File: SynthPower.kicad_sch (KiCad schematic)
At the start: 22 parts, among them IC1 BUF634AIDDAR, IC2 BUF634AIDDAR, IC3 BUF634AIDDAR, J39 Jack-DC, U50 TPS560200, U51 LM1117MP-3.3

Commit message: more work...
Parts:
- C2, C3, C4, C5: footprint Capacitor_SMD:C_0805_2012Metric_Pad1.18x1.45mm_HandSolder -> Capacitor_SMD:C_0805_2012Metric
- C6, C7: footprint Capacitor_SMD:C_0805_2012Metric_Pad1.18x1.45mm_HandSolder -> Capacitor_SMD:C_0603_1608Metric
- R? (x4): footprint Resistor_SMD:R_0805_2012Metric -> Resistor_SMD:R_0603_1608Metric
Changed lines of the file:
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@@
       (effects (font (size 1.27 1.27)))
     )
-    (property "Footprint" "Capacitor_SMD:C_0805_2012Metric_Pad1.18x1.45mm_HandSolder" (at 86.6648 153.035 0)
+    (property "Footprint" "Capacitor_SMD:C_0805_2012Metric" (at 86.6648 153.035 0)
       (effects (font (size 1.27 1.27)) hide)
     )
@@
       (effects (font (size 1.27 1.27)))
     )
-    (property "Footprint" "Capacitor_SMD:C_0805_2012Metric_Pad1.18x1.45mm_HandSolder" (at 86.6648 160.655 0)
+    (property "Footprint" "Capacitor_SMD:C_0805_2012Metric" (at 86.6648 160.655 0)
       (effects (font (size 1.27 1.27)) hide)
     )
@@
       (effects (font (size 1.27 1.27)))
     )
-    (property "Footprint" "Capacitor_SMD:C_0805_2012Metric_Pad1.18x1.45mm_HandSolder" (at 99.3648 153.035 0)
+    (property "Footprint" "Capacitor_SMD:C_0603_1608Metric" (at 99.3648 153.035 0)
       (effects (font (size 1.27 1.27)) hide)
     )
@@
       (effects (font (size 1.27 1.27)))
     )
-    (property "Footprint" "Capacitor_SMD:C_0805_2012Metric_Pad1.18x1.45mm_HandSolder" (at 222.5548 114.3 0)
+    (property "Footprint" "Capacitor_SMD:C_0603_1608Metric" (at 222.5548 114.3 0)
       (effects (font (size 1.27 1.27)) hide)
     )
@@
       (effects (font (size 1.27 1.27)) (justify right))
     )
-    (property "Footprint" "Resistor_SMD:R_0805_2012Metric" (at 66.929 44.196 90)
+    (property "Footprint" "Resistor_SMD:R_0603_1608Metric" (at 66.929 44.196 90)
       (effects (font (size 1.27 1.27)) hide)
     )
@@
       (effects (font (size 1.27 1.27)))
     )
-    (property "Footprint" "Capacitor_SMD:C_0805_2012Metric_Pad1.18x1.45mm_HandSolder" (at 256.2098 114.3 0)
+    (property "Footprint" "Capacitor_SMD:C_0805_2012Metric" (at 256.2098 114.3 0)
       (effects (font (size 1.27 1.27)) hide)
     )
@@
       (effects (font (size 1.27 1.27)))
     )
-    (property "Footprint" "Capacitor_SMD:C_0805_2012Metric_Pad1.18x1.45mm_HandSolder" (at 93.0148 153.035 0)
+    (property "Footprint" "Capacitor_SMD:C_0805_2012Metric" (at 93.0148 153.035 0)
       (effects (font (size 1.27 1.27)) hide)
     )
@@
       (effects (font (size 1.27 1.27)))
     )
-    (property "Footprint" "Resistor_SMD:R_0805_2012Metric" (at 201.676 125.984 90)
+    (property "Footprint" "Resistor_SMD:R_0603_1608Metric" (at 201.676 125.984 90)
       (effects (font (size 1.27 1.27)) hide)
     )
@@
       (effects (font (size 1.27 1.27)))
     )
-    (property "Footprint" "Capacitor_SMD:C_0805_2012Metric_Pad1.18x1.45mm_HandSolder" (at 209.8548 114.3 0)
+    (property "Footprint" "Capacitor_SMD:C_0805_2012Metric" (at 209.8548 114.3 0)
       (effects (font (size 1.27 1.27)) hide)
     )
@@
       (effects (font (size 1.27 1.27)))
     )
-    (property "Footprint" "Capacitor_SMD:C_0805_2012Metric_Pad1.18x1.45mm_HandSolder" (at 99.3648 160.655 0)
+    (property "Footprint" "Capacitor_SMD:C_0603_1608Metric" (at 99.3648 160.655 0)
       (effects (font (size 1.27 1.27)) hide)
     )
@@
       (effects (font (size 1.27 1.27)))
     )
-    (property "Footprint" "Capacitor_SMD:C_0805_2012Metric_Pad1.18x1.45mm_HandSolder" (at 216.2048 114.3 0)
+    (property "Footprint" "Capacitor_SMD:C_0805_2012Metric" (at 216.2048 114.3 0)
       (effects (font (size 1.27 1.27)) hide)
     )
@@
       (effects (font (size 1.27 1.27)) (justify right))
     )
-    (property "Footprint" "Resistor_SMD:R_0805_2012Metric" (at 66.929 51.816 90)
+    (property "Footprint" "Resistor_SMD:R_0603_1608Metric" (at 66.929 51.816 90)
       (effects (font (size 1.27 1.27)) hide)
     )
@@
       (effects (font (size 1.27 1.27)))
     )
-    (property "Footprint" "Resistor_SMD:R_0805_2012Metric" (at 201.676 118.364 90)
+    (property "Footprint" "Resistor_SMD:R_0603_1608Metric" (at 201.676 118.364 90)
       (effects (font (size 1.27 1.27)) hide)
     )
@@
       (effects (font (size 1.27 1.27)))
     )
-    (property "Footprint" "Capacitor_SMD:C_0805_2012Metric_Pad1.18x1.45mm_HandSolder" (at 93.0148 160.655 0)
+    (property "Footprint" "Capacitor_SMD:C_0805_2012Metric" (at 93.0148 160.655 0)
       (effects (font (size 1.27 1.27)) hide)
     )
@@
       (effects (font (size 1.27 1.27)))
     )
-    (property "Footprint" "Capacitor_SMD:C_0805_2012Metric_Pad1.18x1.45mm_HandSolder" (at 263.1948 114.3 0)
-      (effects (font (size 1.27 1.27)) hide)
-    )
+    (property "Footprint" "Capacitor_SMD:C_0805_2012Metric" (at 263.1948 114.3 0)
+      (effects (font (size 1.27 1.27)) hide)
+    )

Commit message: finishing schematic 1.0
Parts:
- added C?: 470nF, Capacitor_SMD:C_0805_2012Metric, symbol Device:C
- added C?: 4.7uF, Capacitor_SMD:C_0805_2012Metric, symbol Device:C
- added TP10, TP11, TP12, TP13, TP7, TP8, TP9: TestPoint, TestPoint:TestPoint_Plated_Hole_D2.0mm, symbol Connector:TestPoint
- J44: renamed from J39; footprint (none) -> Connector_BarrelJack:BarrelJack_CUI_PJ-063AH_Horizontal
- U51: renamed from IC2; footprint SOIC127P600X170-9N -> Package_SO:SOIC-8_3.9x4.9mm_P1.27mm
- U52: renamed from IC3; footprint SOIC127P600X170-9N -> Package_SO:SOIC-8_3.9x4.9mm_P1.27mm
- renumbered C2 to C?, C3 to C?, C6 to C?, C4 to C?, C7 to C?, C5 to C?, IC1 to U50, U50 to U53, U51 to U54
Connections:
- net +12V: now also TP7.1
- net +3V3: now also TP13.1
- net +5V: now also C?.2, C?.2, TP12.1
- net -12V: now also TP9.1
- net GNDD: now also C?.1, C?.1, TP11.1
- net GNDREF: now also TP8.1
- net GNDS: now also TP10.1

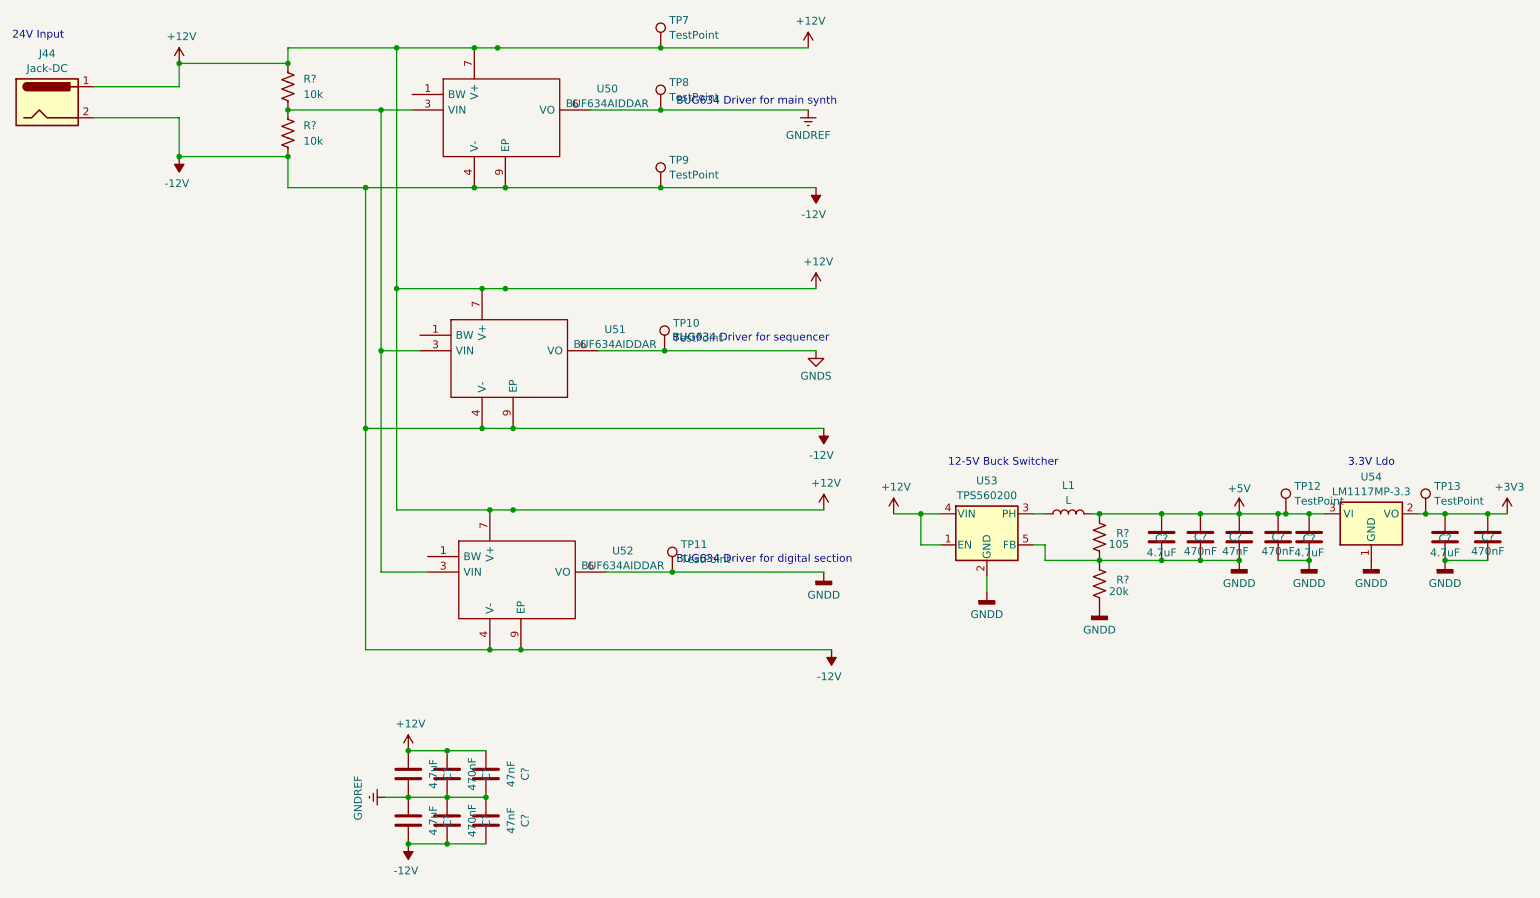
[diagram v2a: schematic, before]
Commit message: doing some routing - split sequencer into another project
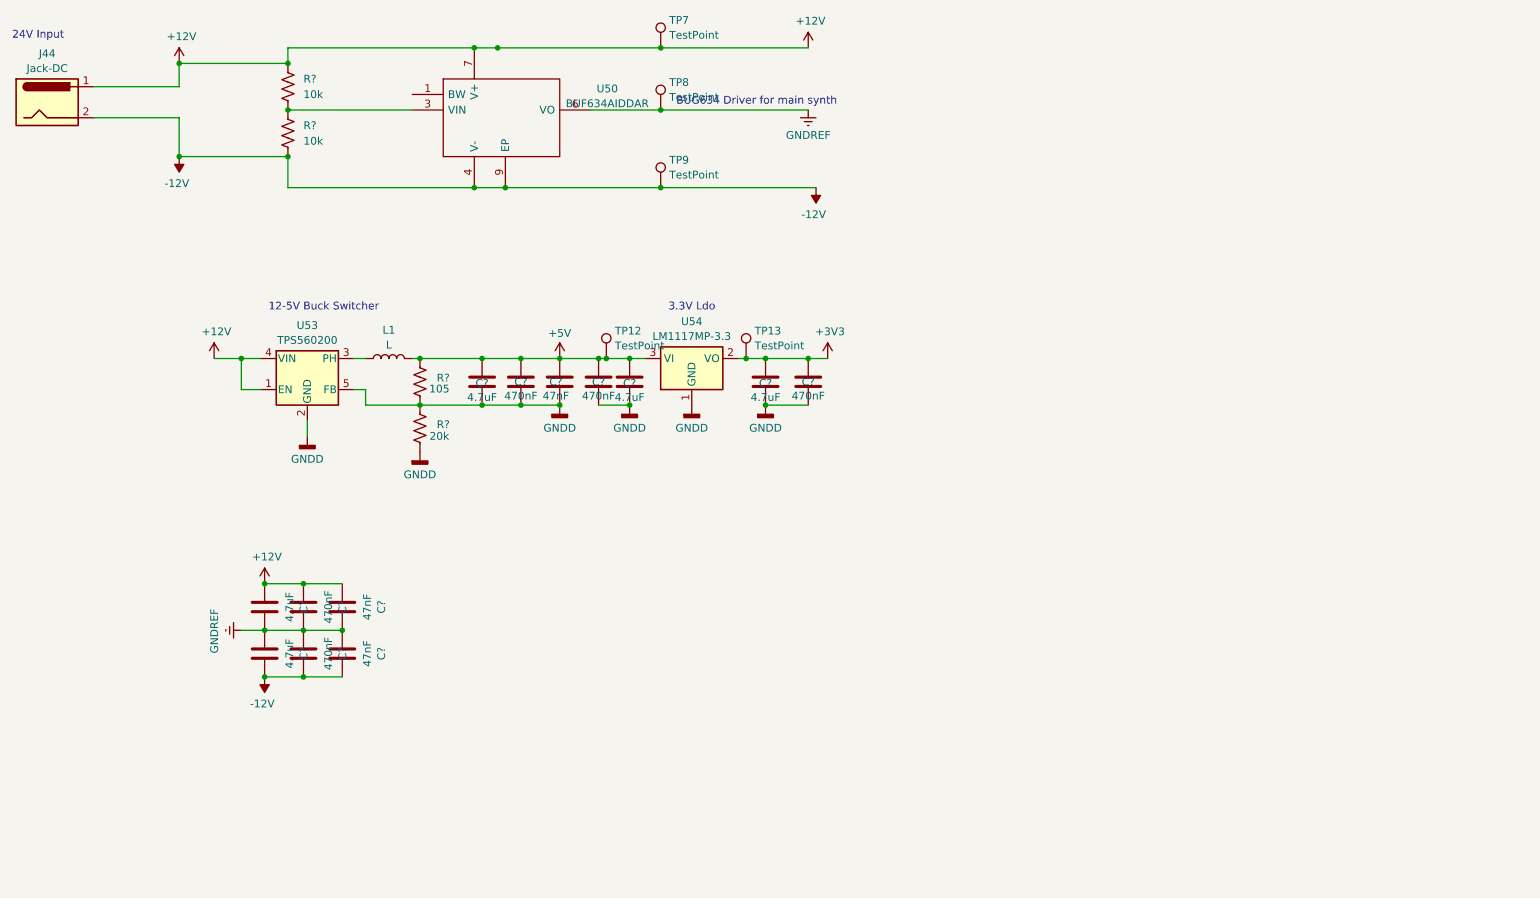
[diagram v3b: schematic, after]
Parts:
- removed TP10, TP11: TestPoint, TestPoint:TestPoint_Plated_Hole_D2.0mm, symbol Connector:TestPoint
- removed U51, U52: BUF634AIDDAR, Package_SO:SOIC-8_3.9x4.9mm_P1.27mm, symbol BUF634AIDDAR:BUF634AIDDAR
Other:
- note removed: "BUG634 Driver for digital section"
- note removed: "BUG634 Driver for sequencer"
- moved on the sheet: C?, L1, R?, TP12, TP13, U53, U54

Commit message: more routing...
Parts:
- U50: footprint SOIC127P600X170-9N -> Package_SO:SOIC-8-1EP_3.9x4.9mm_P1.27mm_EP2.514x3.2mm_ThermalVias
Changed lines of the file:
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@@
       (effects (font (size 1.27 1.27)))
     )
-    (property "Footprint" "SOIC127P600X170-9N" (at 114.935 40.64 0)
+    (property "Footprint" "Package_SO:SOIC-8-1EP_3.9x4.9mm_P1.27mm_EP2.514x3.2mm_ThermalVias" (at 114.935 40.64 0)
       (effects (font (size 1.27 1.27)) (justify left) hide)
     )

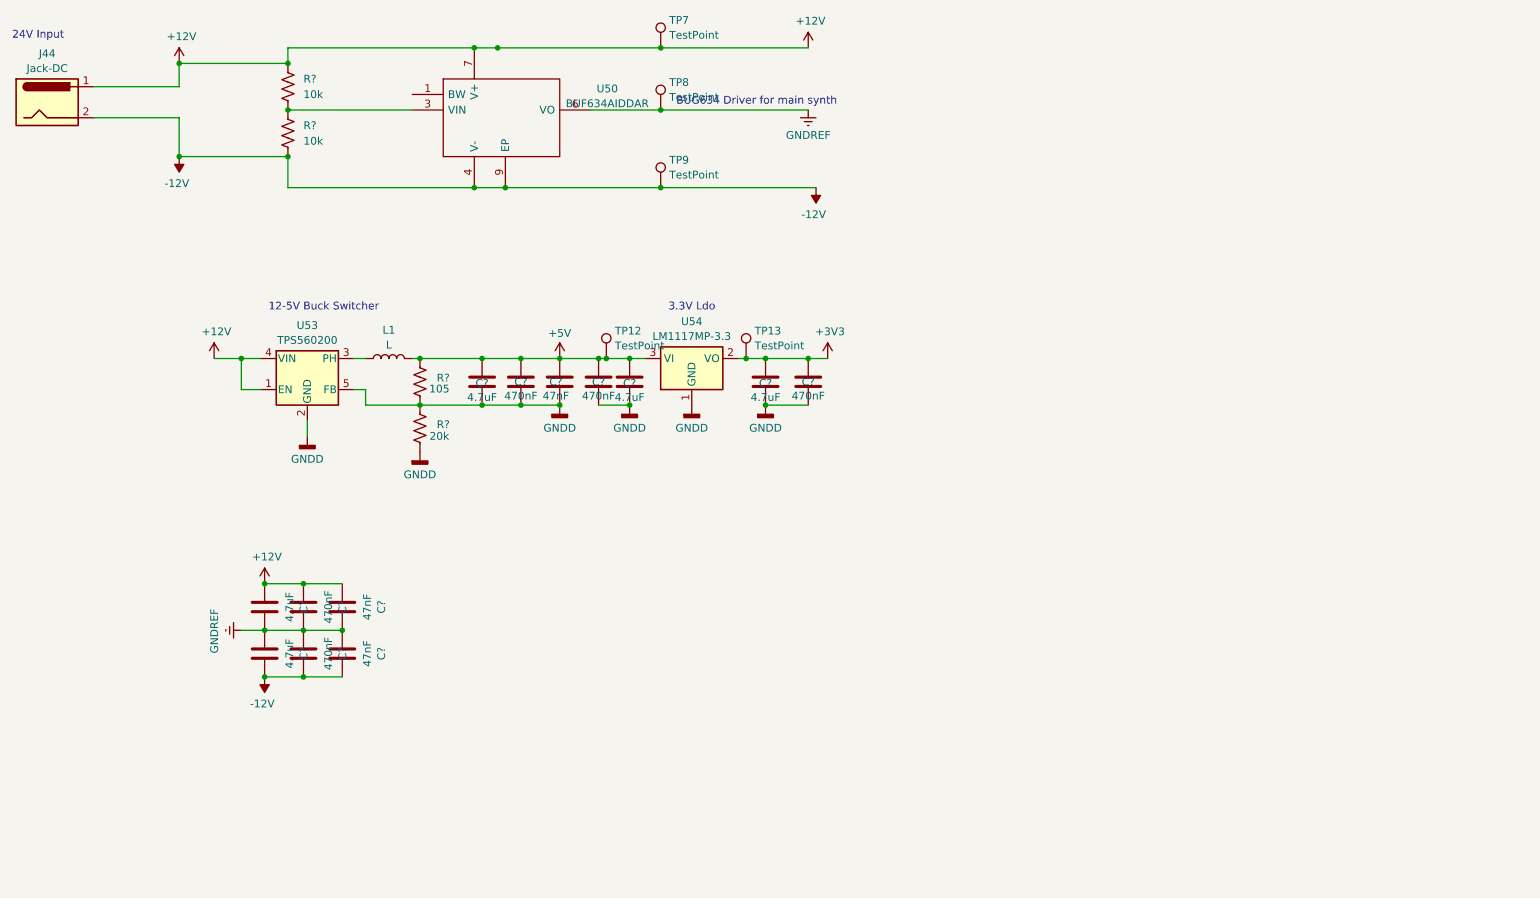
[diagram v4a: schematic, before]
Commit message: lots of routes, added vco3, lfo2.
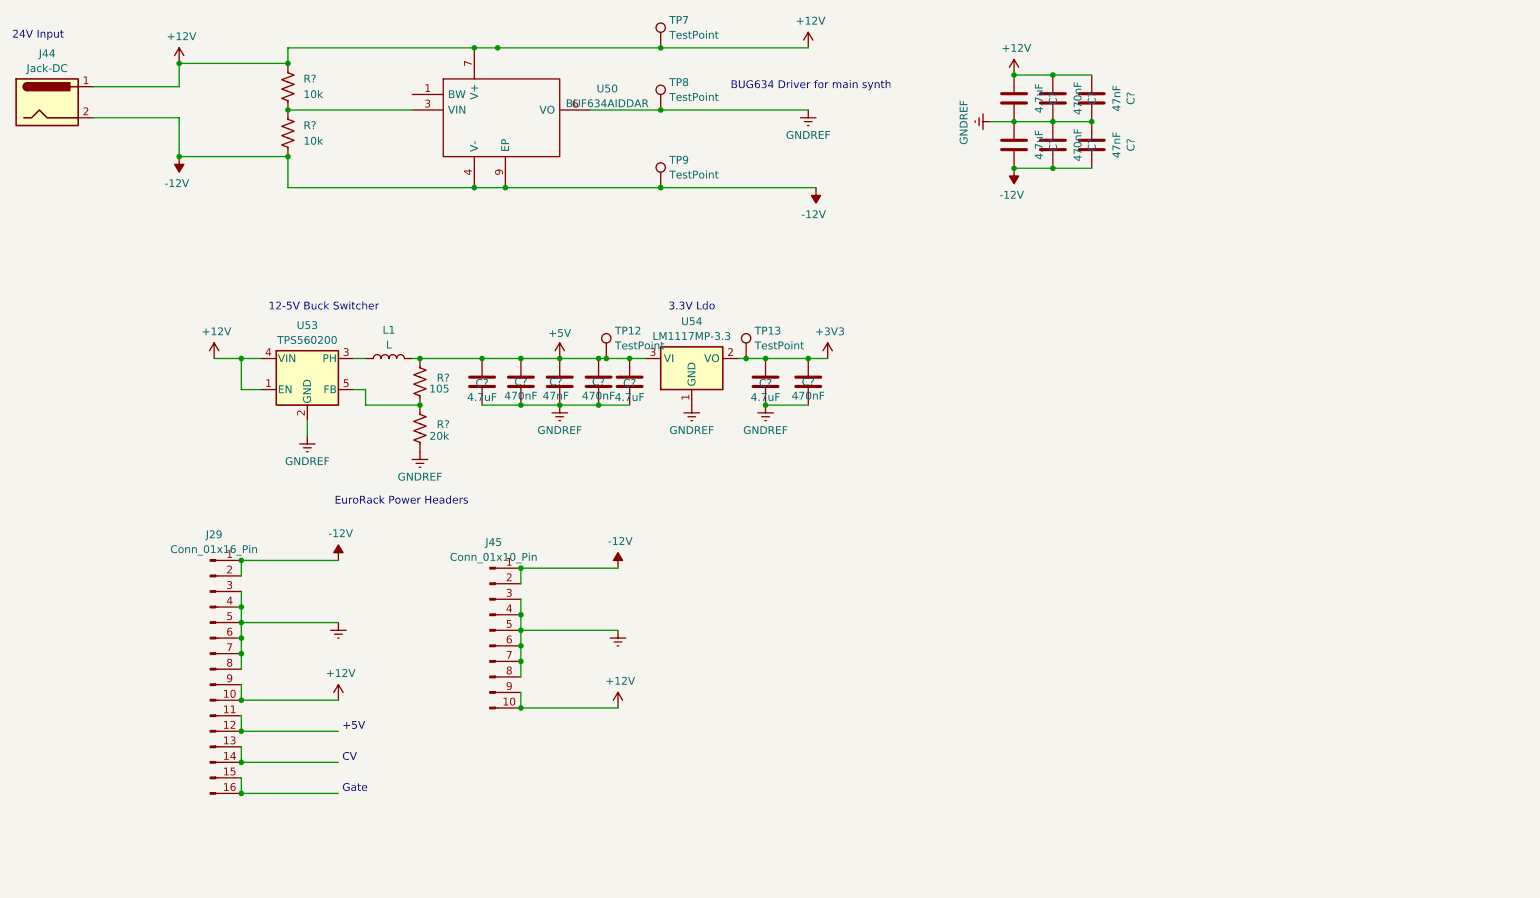
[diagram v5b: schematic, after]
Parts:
- added J29: Conn_01x16_Pin, symbol Connector:Conn_01x16_Pin
- added J45: Conn_01x10_Pin, symbol Connector:Conn_01x10_Pin
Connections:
- net +12V: now also J29.10 (Pin_10), J29.9 (Pin_9), J45.10 (Pin_10), J45.9 (Pin_9)
- net -12V: now also J29.1 (Pin_1), J29.2 (Pin_2), J45.1 (Pin_1), J45.2 (Pin_2)
- net GNDREF: now also C?.1, C?.1, C?.1, C?.1, C?.1, C?.1, C?.1, R?.2, U53.2 (GND), U54.1 (GND), J29.3 (Pin_3), J29.4 (Pin_4), J29.5 (Pin_5), J29.6 (Pin_6), J29.7 (Pin_7), J29.8 (Pin_8), J45.3 (Pin_3), J45.4 (Pin_4), J45.5 (Pin_5), J45.6 (Pin_6), J45.7 (Pin_7), J45.8 (Pin_8)
- removed net GNDD: C?.1, C?.1, C?.1, C?.1, C?.1, C?.1, C?.1, R?.1, R?.2, R?.2, U53.2 (GND), U53.5 (FB), U54.1 (GND)
- new net: J29.11 (Pin_11), J29.12 (Pin_12)
- new net: J29.13 (Pin_13), J29.14 (Pin_14)
- new net: J29.15 (Pin_15), J29.16 (Pin_16)
- new net: R?.1, R?.2, U53.5 (FB)
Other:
- note added: "+5V"
- note added: "CV"
- note added: "EuroRack Power Headers"
- note added: "Gate"
- moved on the sheet: C?
